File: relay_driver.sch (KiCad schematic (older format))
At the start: 7 parts

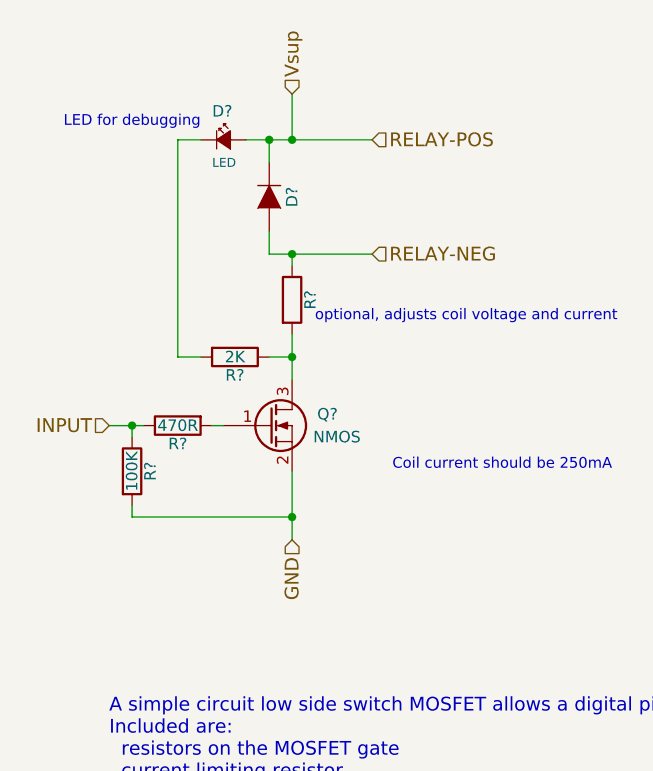
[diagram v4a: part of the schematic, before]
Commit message: added GND fault detect, conns, no pending TODOs
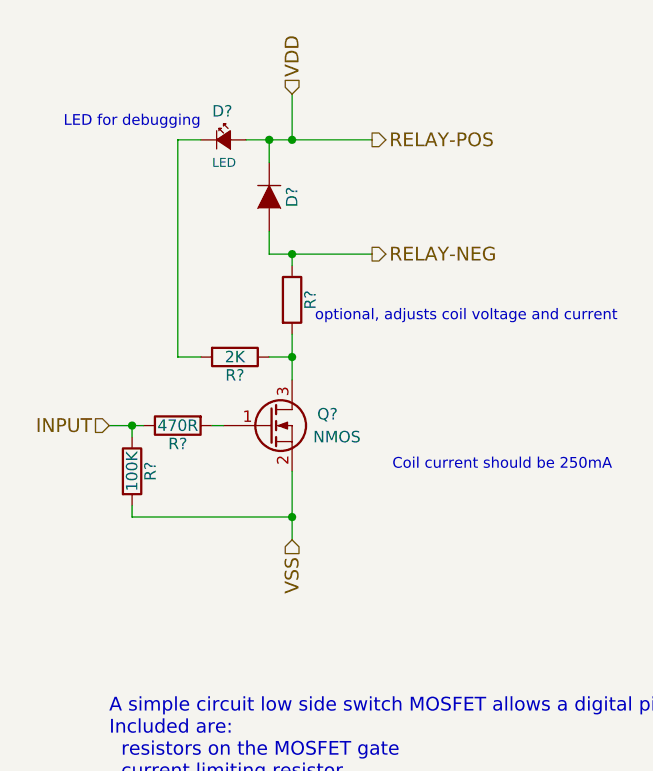
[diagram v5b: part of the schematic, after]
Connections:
- net GND renamed VSS
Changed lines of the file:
@@
 $Descr User 7874 5906
 encoding utf-8
-Sheet 2 5
+Sheet 5 5
 Title ""
 Date ""
@@
 AR Path="/5728B2EB/57284B32" Ref="Q?"  Part="1"
 AR Path="/5728BD96/57284B32" Ref="Q?"  Part="1"
+AR Path="/5736E780/57284B32" Ref="Q?"  Part="1"
 F 0 "Q?" H 4200 3100 50  0000 R CNN
 F 1 "NMOS" H 4300 3000 50  0000 R CNN
@@
 AR Path="/5728B2EB/57284C7E" Ref="R?"  Part="1"
 AR Path="/5728BD96/57284C7E" Ref="R?"  Part="1"
+AR Path="/5736E780/57284C7E" Ref="R?"  Part="1"
 F 0 "R?" V 3380 3250 50  0000 C CNN
 F 1 "100K" V 3300 3250 50  0000 C CNN
@@
 AR Path="/5728B2EB/57284CE3" Ref="R?"  Part="1"
 AR Path="/5728BD96/57284CE3" Ref="R?"  Part="1"
+AR Path="/5736E780/57284CE3" Ref="R?"  Part="1"
 F 0 "R?" V 3580 3050 50  0000 C CNN
 F 1 "470R" V 3500 3050 50  0000 C CNN
@@
 AR Path="/5728B2EB/5728508D" Ref="D?"  Part="1"
 AR Path="/5728BD96/5728508D" Ref="D?"  Part="1"
+AR Path="/5736E780/5728508D" Ref="D?"  Part="1"
 F 0 "D?" H 3900 2150 50  0000 C CNN
 F 1 "D" H 3900 1950 50  0001 C CNN
@@
 $EndComp
 Wire Wire Line
-	3900 2300 4000 2300
-Wire Wire Line
-	4000 2300 4350 2300
+	3900 2300 4350 2300
 Wire Wire Line
 	3900 2300 3900 2200
@@
 AR Path="/5728B2EB/5728580D" Ref="R?"  Part="1"
 AR Path="/5728BD96/5728580D" Ref="R?"  Part="1"
+AR Path="/5736E780/5728580D" Ref="R?"  Part="1"
 F 0 "R?" V 4080 2500 50  0000 C CNN
 F 1 "R" V 4000 2500 50  0001 C CNN
@@
 $EndComp
 Wire Wire Line
-	4000 2850 4000 2750
-Wire Wire Line
-	4000 2750 4000 2650
+	4000 2650 4000 2850
 Text Notes 3550 5150 0    60   ~ 0
 Relay Driver Sub-Circuit
@@
 A simple circuit low side switch MOSFET allows a digital pin to drive the coil of a relay.\nIncluded are:\n  resistors on the MOSFET gate\n  current limiting resistor\n  flyback diode
 Wire Wire Line
-	4000 3250 4000 3450
-Wire Wire Line
-	4000 3450 4000 3550
+	4000 3250 4000 3550
 Wire Wire Line
 	4000 3450 3300 3450
@@
 	3650 3050 3700 3050
 Wire Wire Line
-	3200 3050 3300 3050
-Wire Wire Line
-	3300 3050 3350 3050
+	3200 3050 3350 3050
 Wire Wire Line
 	3300 3050 3300 3100
@@
 Connection ~ 4000 3450
 Text HLabel 4000 3550 3    60   Input ~ 0
-GND
+VSS
 Connection ~ 3300 3050
 Text HLabel 3200 3050 0    60   Input ~ 0
 INPUT
 Text HLabel 4000 1600 1    60   Input ~ 0
-Vsup
-Text HLabel 4350 1800 2    60   Input ~ 0
+VDD
+Text HLabel 4350 1800 2    60   Output ~ 0
 RELAY-POS
-Text HLabel 4350 2300 2    60   Input ~ 0
+Text HLabel 4350 2300 2    60   Output ~ 0
 RELAY-NEG
 Wire Wire Line
-	3800 1800 3900 1800
-Wire Wire Line
-	3900 1800 4000 1800
-Wire Wire Line
-	4000 1800 4350 1800
+	3800 1800 4350 1800
 Wire Wire Line
 	4000 1600 4000 1800
@@
 U 1 1 573F0404
 P 3700 1800
+AR Path="/572843F5/573F0404" Ref="D?"  Part="1"
+AR Path="/5728B2EB/573F0404" Ref="D?"  Part="1"
+AR Path="/5728BD96/573F0404" Ref="D?"  Part="1"
+AR Path="/5736E780/573F0404" Ref="D?"  Part="1"
 F 0 "D?" H 3650 1925 50  0000 L CNN
 F 1 "LED" H 3650 1700 39  0000 L CNN
@@
 U 1 1 573F0488
 P 3750 2750
+AR Path="/572843F5/573F0488" Ref="R?"  Part="1"
+AR Path="/5728B2EB/573F0488" Ref="R?"  Part="1"
+AR Path="/5728BD96/573F0488" Ref="R?"  Part="1"
+AR Path="/5736E780/573F0488" Ref="R?"  Part="1"
 F 0 "R?" V 3830 2750 50  0000 C CNN
 F 1 "2K" V 3750 2750 50  0000 C CNN

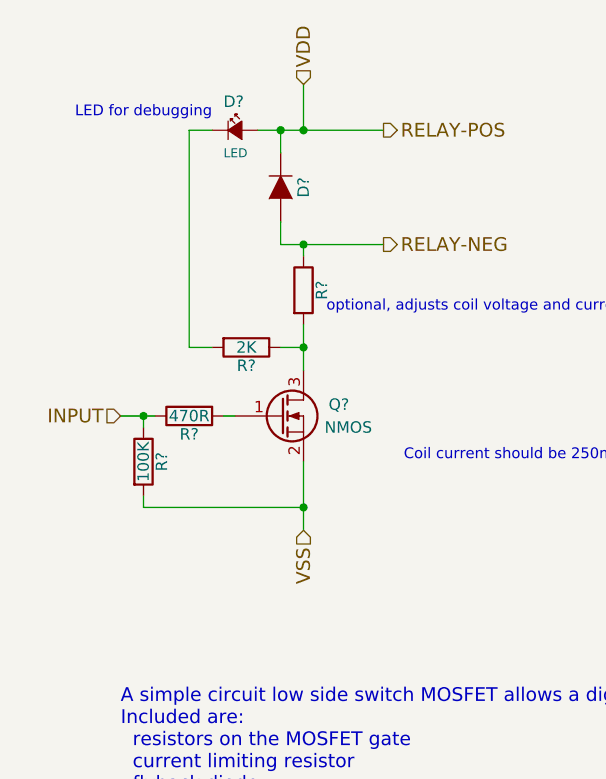
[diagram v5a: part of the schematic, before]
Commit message: BMS added ctrl pins, both fault outputs to MCU, ...
added a few more comments for component selection

directions on net labels
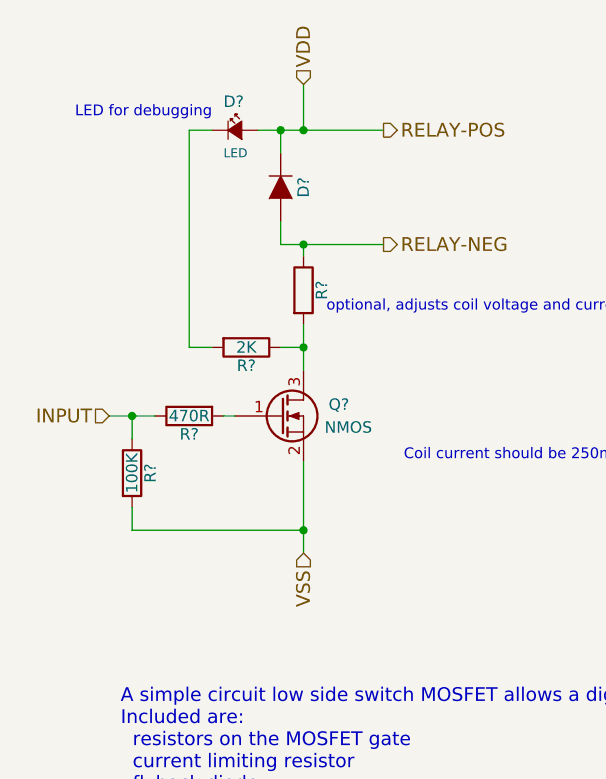
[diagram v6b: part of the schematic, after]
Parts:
- Q?: Imax (none) -> 500mA; Vgs Thresh (none) -> < 3V
- R?: Power (none) -> 1W
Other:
- moved on the sheet: R?
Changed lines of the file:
@@
 EESchema Schematic File Version 2
+LIBS:rloopPowerNode-rescue
 LIBS:power
 LIBS:device
@@
 F 2 "" H 4100 3150 50  0000 C CNN
 F 3 "" H 3900 3050 50  0000 C CNN
+F 4 "< 3V" H 3900 3050 60  0001 C CNN "Vgs Thresh"
+F 5 "500mA" H 3900 3050 60  0001 C CNN "Imax"
 	1    3900 3050
 	1    0    0    -1
@@
 L R R?
 U 1 1 57284C7E
-P 3300 3250
+P 3250 3300
 AR Path="/572843F5/57284C7E" Ref="R?"  Part="1"
 AR Path="/5728BD9D/57284C7E" Ref="R?"  Part="1"
@@
 AR Path="/5728BD96/57284C7E" Ref="R?"  Part="1"
 AR Path="/5736E780/57284C7E" Ref="R?"  Part="1"
-F 0 "R?" V 3380 3250 50  0000 C CNN
-F 1 "100K" V 3300 3250 50  0000 C CNN
-F 2 "" V 3230 3250 50  0000 C CNN
-F 3 "" H 3300 3250 50  0000 C CNN
-	1    3300 3250
+F 0 "R?" V 3330 3300 50  0000 C CNN
+F 1 "100K" V 3250 3300 50  0000 C CNN
+F 2 "" V 3180 3300 50  0000 C CNN
+F 3 "" H 3250 3300 50  0000 C CNN
+	1    3250 3300
 	1    0    0    -1
 $EndComp
@@
 $EndComp
 Wire Wire Line
-	3900 2300 4350 2300
+	3900 2300 4000 2300
+Wire Wire Line
+	4000 2300 4350 2300
 Wire Wire Line
 	3900 2300 3900 2200
@@
 F 2 "Resistors_SMD:R_1206_HandSoldering" V 3930 2500 50  0001 C CNN
 F 3 "" H 4000 2500 50  0000 C CNN
+F 4 "1W" V 4000 2500 60  0001 C CNN "Power"
 	1    4000 2500
 	1    0    0    -1
 $EndComp
 Wire Wire Line
-	4000 2650 4000 2850
+	4000 2650 4000 2750
+Wire Wire Line
+	4000 2750 4000 2850
 Text Notes 3550 5150 0    60   ~ 0
 Relay Driver Sub-Circuit
@@
 	4000 3250 4000 3550
 Wire Wire Line
-	4000 3450 3300 3450
+	4000 3550 4000 3650
 Wire Wire Line
-	3300 3450 3300 3400
+	4000 3550 3250 3550
+Wire Wire Line
+	3250 3550 3250 3450
 Wire Wire Line
 	3650 3050 3700 3050
 Wire Wire Line
-	3200 3050 3350 3050
+	3150 3050 3250 3050
 Wire Wire Line
-	3300 3050 3300 3100
+	3250 3050 3350 3050
+Wire Wire Line
+	3250 3050 3250 3150
 Wire Wire Line
 	4000 2350 4000 2300
-Connection ~ 4000 3450
-Text HLabel 4000 3550 3    60   Input ~ 0
+Connection ~ 4000 3550
+Text HLabel 4000 3650 3    60   Input ~ 0
 VSS
-Connection ~ 3300 3050
-Text HLabel 3200 3050 0    60   Input ~ 0
+Connection ~ 3250 3050
+Text HLabel 3150 3050 0    60   Input ~ 0
 INPUT
 Text HLabel 4000 1600 1    60   Input ~ 0
@@
 RELAY-NEG
 Wire Wire Line
-	3800 1800 4350 1800
+	3800 1800 3900 1800
+Wire Wire Line
+	3900 1800 4000 1800
+Wire Wire Line
+	4000 1800 4350 1800
 Wire Wire Line
 	4000 1600 4000 1800

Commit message: added footprint
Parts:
- D12: renamed from D?; footprint (none) -> LEDs:LED_0603
- D13: renamed from D?; footprint (none) -> Diodes_SMD:SOD-123
- Q4: renamed from Q?; footprint (none) -> TO_SOT_Packages_SMD:SOT-23
- R22: renamed from R?; footprint Resistors_SMD:R_1206_HandSoldering -> Resistors_SMD:R_1210_HandSoldering
- R23: renamed from R?; footprint Resistors_SMD:R_1206_HandSoldering -> Resistors_SMD:R_0603
- R24, R25: renamed from R?; footprint (none) -> Resistors_SMD:R_0603
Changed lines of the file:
@@
 $EndDescr
 $Comp
-L Q_NMOS_GSD Q?
+L Q_NMOS_GSD Q4
 U 1 1 57284B32
 P 3900 3050
-AR Path="/572843F5/57284B32" Ref="Q?"  Part="1"
-AR Path="/5728BD9D/57284B32" Ref="Q?"  Part="1"
-AR Path="/5728B2EB/57284B32" Ref="Q?"  Part="1"
-AR Path="/5728BD96/57284B32" Ref="Q?"  Part="1"
-AR Path="/5736E780/57284B32" Ref="Q?"  Part="1"
-F 0 "Q?" H 4200 3100 50  0000 R CNN
+AR Path="/572843F5/57284B32" Ref="Q4"  Part="1"
+AR Path="/5728B2EB/57284B32" Ref="Q5"  Part="1"
+AR Path="/5728BD96/57284B32" Ref="Q6"  Part="1"
+AR Path="/5736E780/57284B32" Ref="Q7"  Part="1"
+F 0 "Q7" H 4200 3100 50  0000 R CNN
 F 1 "NMOS" H 4300 3000 50  0000 R CNN
-F 2 "" H 4100 3150 50  0000 C CNN
+F 2 "TO_SOT_Packages_SMD:SOT-23" H 4100 3150 50  0001 C CNN
 F 3 "" H 3900 3050 50  0000 C CNN
 F 4 "< 3V" H 3900 3050 60  0001 C CNN "Vgs Thresh"
@@
 $EndComp
 $Comp
-L R R?
+L R R25
 U 1 1 57284C7E
 P 3250 3300
-AR Path="/572843F5/57284C7E" Ref="R?"  Part="1"
-AR Path="/5728BD9D/57284C7E" Ref="R?"  Part="1"
-AR Path="/5728B2EB/57284C7E" Ref="R?"  Part="1"
-AR Path="/5728BD96/57284C7E" Ref="R?"  Part="1"
-AR Path="/5736E780/57284C7E" Ref="R?"  Part="1"
-F 0 "R?" V 3330 3300 50  0000 C CNN
+AR Path="/572843F5/57284C7E" Ref="R25"  Part="1"
+AR Path="/5728B2EB/57284C7E" Ref="R29"  Part="1"
+AR Path="/5728BD96/57284C7E" Ref="R33"  Part="1"
+AR Path="/5736E780/57284C7E" Ref="R37"  Part="1"
+F 0 "R37" V 3330 3300 50  0000 C CNN
 F 1 "100K" V 3250 3300 50  0000 C CNN
-F 2 "" V 3180 3300 50  0000 C CNN
+F 2 "Resistors_SMD:R_0603" V 3180 3300 50  0001 C CNN
 F 3 "" H 3250 3300 50  0000 C CNN
 	1    3250 3300
@@
 $EndComp
 $Comp
-L R R?
+L R R24
 U 1 1 57284CE3
 P 3500 3050
-AR Path="/572843F5/57284CE3" Ref="R?"  Part="1"
-AR Path="/5728BD9D/57284CE3" Ref="R?"  Part="1"
-AR Path="/5728B2EB/57284CE3" Ref="R?"  Part="1"
-AR Path="/5728BD96/57284CE3" Ref="R?"  Part="1"
-AR Path="/5736E780/57284CE3" Ref="R?"  Part="1"
-F 0 "R?" V 3580 3050 50  0000 C CNN
+AR Path="/572843F5/57284CE3" Ref="R24"  Part="1"
+AR Path="/5728B2EB/57284CE3" Ref="R28"  Part="1"
+AR Path="/5728BD96/57284CE3" Ref="R32"  Part="1"
+AR Path="/5736E780/57284CE3" Ref="R36"  Part="1"
+F 0 "R36" V 3580 3050 50  0000 C CNN
 F 1 "470R" V 3500 3050 50  0000 C CNN
-F 2 "" V 3430 3050 50  0000 C CNN
+F 2 "Resistors_SMD:R_0603" V 3430 3050 50  0001 C CNN
 F 3 "" H 3500 3050 50  0000 C CNN
 	1    3500 3050
@@
 $EndComp
 $Comp
-L D D?
+L D D13
 U 1 1 5728508D
 P 3900 2050
-AR Path="/572843F5/5728508D" Ref="D?"  Part="1"
-AR Path="/5728BD9D/5728508D" Ref="D?"  Part="1"
-AR Path="/5728B2EB/5728508D" Ref="D?"  Part="1"
-AR Path="/5728BD96/5728508D" Ref="D?"  Part="1"
-AR Path="/5736E780/5728508D" Ref="D?"  Part="1"
-F 0 "D?" H 3900 2150 50  0000 C CNN
+AR Path="/572843F5/5728508D" Ref="D13"  Part="1"
+AR Path="/5728B2EB/5728508D" Ref="D15"  Part="1"
+AR Path="/5728BD96/5728508D" Ref="D17"  Part="1"
+AR Path="/5736E780/5728508D" Ref="D19"  Part="1"
+F 0 "D19" H 3900 2150 50  0000 C CNN
 F 1 "D" H 3900 1950 50  0001 C CNN
-F 2 "" H 3900 2050 50  0000 C CNN
+F 2 "Diodes_SMD:SOD-123" H 3900 2050 50  0001 C CNN
 F 3 "" H 3900 2050 50  0000 C CNN
 	1    3900 2050
@@
 $EndComp
 Wire Wire Line
-	3900 2300 4000 2300
-Wire Wire Line
-	4000 2300 4350 2300
+	3900 2300 4350 2300
 Wire Wire Line
 	3900 2300 3900 2200
@@
 	3900 1900 3900 1800
 $Comp
-L R R?
+L R R22
 U 1 1 5728580D
 P 4000 2500
-AR Path="/572843F5/5728580D" Ref="R?"  Part="1"
-AR Path="/5728BD9D/5728580D" Ref="R?"  Part="1"
-AR Path="/5728B2EB/5728580D" Ref="R?"  Part="1"
-AR Path="/5728BD96/5728580D" Ref="R?"  Part="1"
-AR Path="/5736E780/5728580D" Ref="R?"  Part="1"
-F 0 "R?" V 4080 2500 50  0000 C CNN
+AR Path="/572843F5/5728580D" Ref="R22"  Part="1"
+AR Path="/5728B2EB/5728580D" Ref="R26"  Part="1"
+AR Path="/5728BD96/5728580D" Ref="R30"  Part="1"
+AR Path="/5736E780/5728580D" Ref="R34"  Part="1"
+F 0 "R34" V 4080 2500 50  0000 C CNN
 F 1 "R" V 4000 2500 50  0001 C CNN
-F 2 "Resistors_SMD:R_1206_HandSoldering" V 3930 2500 50  0001 C CNN
+F 2 "Resistors_SMD:R_1210_HandSoldering" V 3930 2500 50  0001 C CNN
 F 3 "" H 4000 2500 50  0000 C CNN
 F 4 "1W" V 4000 2500 60  0001 C CNN "Power"
@@
 $EndComp
 Wire Wire Line
-	4000 2650 4000 2750
-Wire Wire Line
-	4000 2750 4000 2850
+	4000 2650 4000 2850
 Text Notes 3550 5150 0    60   ~ 0
 Relay Driver Sub-Circuit
@@
 A simple circuit low side switch MOSFET allows a digital pin to drive the coil of a relay.\nIncluded are:\n  resistors on the MOSFET gate\n  current limiting resistor\n  flyback diode
 Wire Wire Line
-	4000 3250 4000 3550
-Wire Wire Line
-	4000 3550 4000 3650
+	4000 3250 4000 3650
 Wire Wire Line
 	4000 3550 3250 3550
@@
 	3650 3050 3700 3050
 Wire Wire Line
-	3150 3050 3250 3050
-Wire Wire Line
-	3250 3050 3350 3050
+	3150 3050 3350 3050
 Wire Wire Line
 	3250 3050 3250 3150
@@
 RELAY-NEG
 Wire Wire Line
-	3800 1800 3900 1800
-Wire Wire Line
-	3900 1800 4000 1800
-Wire Wire Line
-	4000 1800 4350 1800
+	3800 1800 4350 1800
 Wire Wire Line
 	4000 1600 4000 1800
 Connection ~ 4000 1800
 $Comp
-L Led_Small D?
+L Led_Small D12
 U 1 1 573F0404
 P 3700 1800
-AR Path="/572843F5/573F0404" Ref="D?"  Part="1"
-AR Path="/5728B2EB/573F0404" Ref="D?"  Part="1"
-AR Path="/5728BD96/573F0404" Ref="D?"  Part="1"
-AR Path="/5736E780/573F0404" Ref="D?"  Part="1"
-F 0 "D?" H 3650 1925 50  0000 L CNN
+AR Path="/572843F5/573F0404" Ref="D12"  Part="1"
+AR Path="/5728B2EB/573F0404" Ref="D14"  Part="1"
+AR Path="/5728BD96/573F0404" Ref="D16"  Part="1"
+AR Path="/5736E780/573F0404" Ref="D18"  Part="1"
+F 0 "D18" H 3650 1925 50  0000 L CNN
 F 1 "LED" H 3650 1700 39  0000 L CNN
-F 2 "" V 3700 1800 50  0000 C CNN
+F 2 "LEDs:LED_0603" V 3700 1800 50  0001 C CNN
 F 3 "" V 3700 1800 50  0000 C CNN
 	1    3700 1800
@@
 $EndComp
 $Comp
-L R R?
+L R R23
 U 1 1 573F0488
 P 3750 2750
-AR Path="/572843F5/573F0488" Ref="R?"  Part="1"
-AR Path="/5728B2EB/573F0488" Ref="R?"  Part="1"
-AR Path="/5728BD96/573F0488" Ref="R?"  Part="1"
-AR Path="/5736E780/573F0488" Ref="R?"  Part="1"
-F 0 "R?" V 3830 2750 50  0000 C CNN
+AR Path="/572843F5/573F0488" Ref="R23"  Part="1"
+AR Path="/5728B2EB/573F0488" Ref="R27"  Part="1"
+AR Path="/5728BD96/573F0488" Ref="R31"  Part="1"
+AR Path="/5736E780/573F0488" Ref="R35"  Part="1"
+F 0 "R35" V 3830 2750 50  0000 C CNN
 F 1 "2K" V 3750 2750 50  0000 C CNN
-F 2 "Resistors_SMD:R_1206_HandSoldering" V 3680 2750 50  0001 C CNN
+F 2 "Resistors_SMD:R_0603" V 3680 2750 50  0001 C CNN
 F 3 "" H 3750 2750 50  0000 C CNN
 	1    3750 2750

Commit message: more parts assigned
just a check in for the meeting
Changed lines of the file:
@@
 AR Path="/5728BD96/57284B32" Ref="Q6"  Part="1"
 AR Path="/5736E780/57284B32" Ref="Q7"  Part="1"
-F 0 "Q7" H 4200 3100 50  0000 R CNN
+F 0 "Q5" H 4200 3100 50  0000 R CNN
 F 1 "NMOS" H 4300 3000 50  0000 R CNN
 F 2 "TO_SOT_Packages_SMD:SOT-23" H 4100 3150 50  0001 C CNN
@@
 AR Path="/5728BD96/57284C7E" Ref="R33"  Part="1"
 AR Path="/5736E780/57284C7E" Ref="R37"  Part="1"
-F 0 "R37" V 3330 3300 50  0000 C CNN
+F 0 "R29" V 3330 3300 50  0000 C CNN
 F 1 "100K" V 3250 3300 50  0000 C CNN
 F 2 "Resistors_SMD:R_0603" V 3180 3300 50  0001 C CNN
@@
 AR Path="/5728BD96/57284CE3" Ref="R32"  Part="1"
 AR Path="/5736E780/57284CE3" Ref="R36"  Part="1"
-F 0 "R36" V 3580 3050 50  0000 C CNN
+F 0 "R28" V 3580 3050 50  0000 C CNN
 F 1 "470R" V 3500 3050 50  0000 C CNN
 F 2 "Resistors_SMD:R_0603" V 3430 3050 50  0001 C CNN
@@
 AR Path="/5728BD96/5728508D" Ref="D17"  Part="1"
 AR Path="/5736E780/5728508D" Ref="D19"  Part="1"
-F 0 "D19" H 3900 2150 50  0000 C CNN
+F 0 "D15" H 3900 2150 50  0000 C CNN
 F 1 "D" H 3900 1950 50  0001 C CNN
 F 2 "Diodes_SMD:SOD-123" H 3900 2050 50  0001 C CNN
@@
 AR Path="/5728BD96/5728580D" Ref="R30"  Part="1"
 AR Path="/5736E780/5728580D" Ref="R34"  Part="1"
-F 0 "R34" V 4080 2500 50  0000 C CNN
+F 0 "R26" V 4080 2500 50  0000 C CNN
 F 1 "R" V 4000 2500 50  0001 C CNN
 F 2 "Resistors_SMD:R_1210_HandSoldering" V 3930 2500 50  0001 C CNN
@@
 AR Path="/5728BD96/573F0404" Ref="D16"  Part="1"
 AR Path="/5736E780/573F0404" Ref="D18"  Part="1"
-F 0 "D18" H 3650 1925 50  0000 L CNN
+F 0 "D14" H 3650 1925 50  0000 L CNN
 F 1 "LED" H 3650 1700 39  0000 L CNN
 F 2 "LEDs:LED_0603" V 3700 1800 50  0001 C CNN
@@
 AR Path="/5728BD96/573F0488" Ref="R31"  Part="1"
 AR Path="/5736E780/573F0488" Ref="R35"  Part="1"
-F 0 "R35" V 3830 2750 50  0000 C CNN
+F 0 "R27" V 3830 2750 50  0000 C CNN
 F 1 "2K" V 3750 2750 50  0000 C CNN
 F 2 "Resistors_SMD:R_0603" V 3680 2750 50  0001 C CNN
